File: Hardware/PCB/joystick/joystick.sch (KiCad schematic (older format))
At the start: 38 parts, among them J1 Synth_power_2x5, J2 3_pin_Molex_connector, J3 2_pin_Molex_connector, J4 AudioJack2, J5 6 pin Molex header, J6 AudioJack2, J7 3_pin_Molex_header, J8 2_pin_Molex_header, U1 TL074

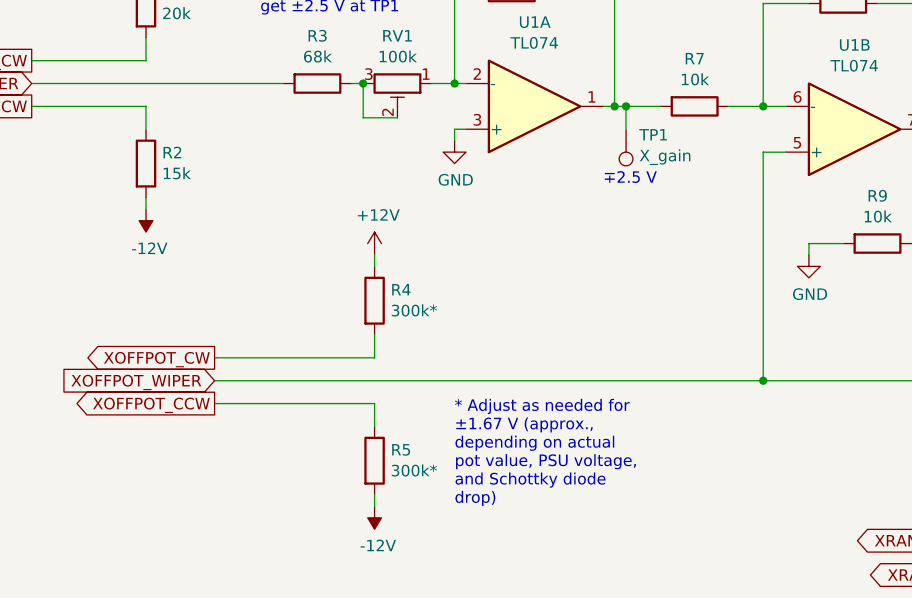
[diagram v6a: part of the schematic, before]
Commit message: Correct resistor value
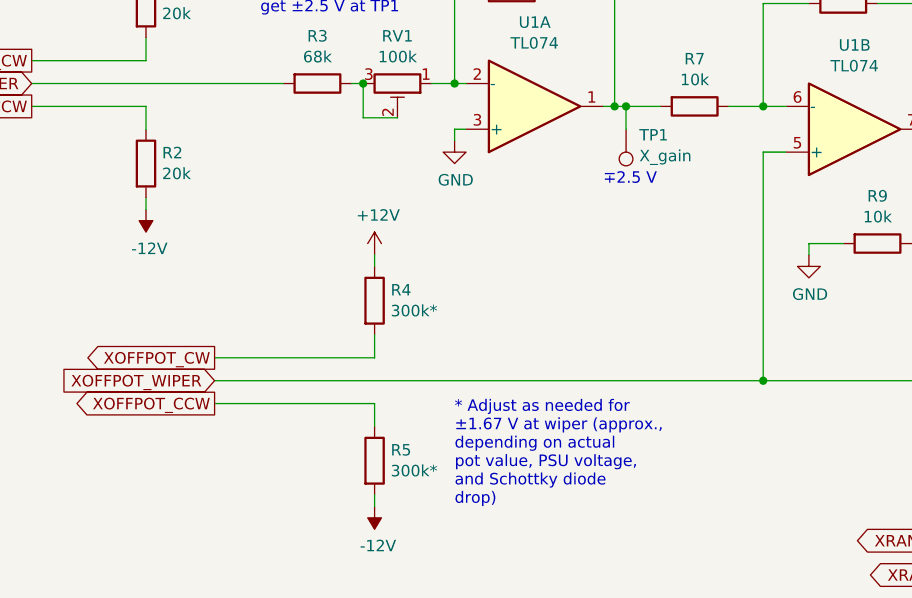
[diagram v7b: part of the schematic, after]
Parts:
- R2: value 15k -> 20k
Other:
- note added: "* Adjust as needed for\n±1.67 V at wiper (approx.,\ndepending on actual\npot value, PSU voltage,\nand Schottky diode\ndrop)"
- note removed: "* Adjust as needed for\n±1.67 V (approx.,\ndepending on actual\npot value, PSU voltage,\nand Schottky diode\ndrop)"
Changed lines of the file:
@@
 P 1600 2350
 F 0 "R2" H 1670 2396 50  0000 L CNN
-F 1 "15k" H 1670 2305 50  0000 L CNN
+F 1 "20k" H 1670 2305 50  0000 L CNN
 F 2 "ao_tht:R_Axial_DIN0207_L6.3mm_D2.5mm_P10.16mm_Horizontal" V 1530 2350 50  0001 C CNN
 F 3 "~" H 1600 2350 50  0001 C CNN
@@
 Check pot for reasonably\naccurate 100k from \npin 1 to 3 or compensate\nby adjusting fixed\nresistors.\n
 Text Notes 2950 3850 0    50   ~ 0
-* Adjust as needed for\n±1.67 V (approx.,\ndepending on actual\npot value, PSU voltage,\nand Schottky diode\ndrop)
+* Adjust as needed for\n±1.67 V at wiper (approx.,\ndepending on actual\npot value, PSU voltage,\nand Schottky diode\ndrop)
 $EndSCHEMATC

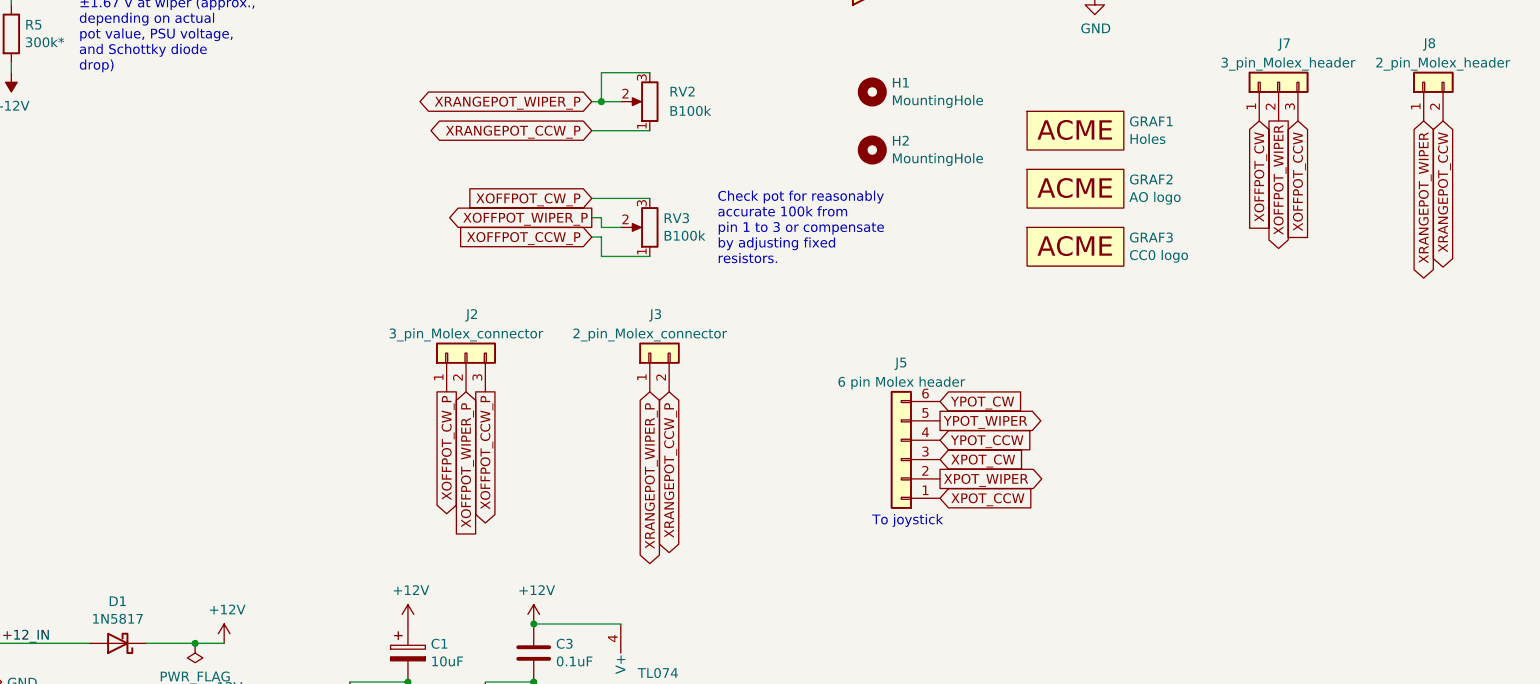
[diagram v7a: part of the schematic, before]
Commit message: Fix wrong R value; update documentation; images
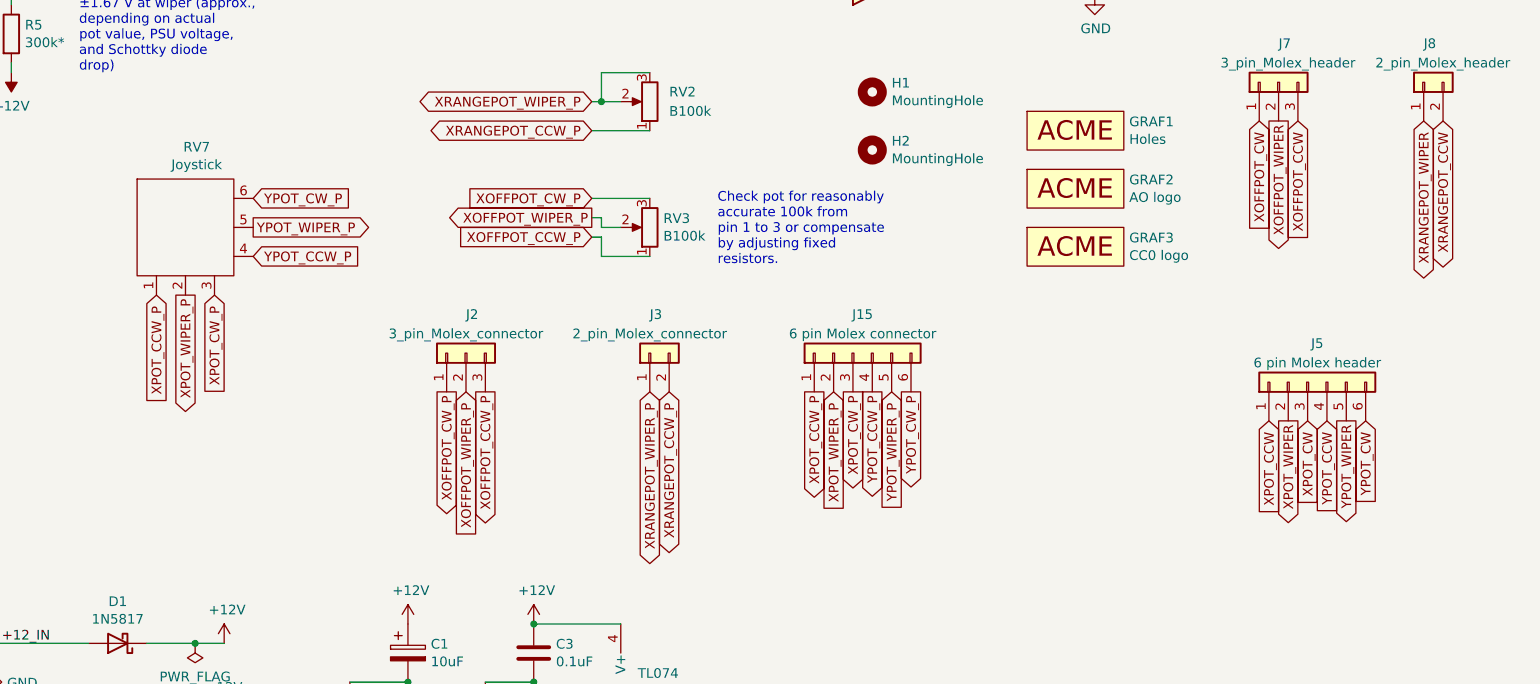
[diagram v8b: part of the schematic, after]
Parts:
- added J15: 6 pin Molex connector, Connector_Molex:Molex_KK-254_AE-6410-06A_1x06_P2.54mm_Vertical, symbol Connector_Generic:Conn_01x06
- added RV7: Joystick, symbol joystick:Joystick
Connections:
- new net XPOT_CCW_P: J15.1 (Pin_1), RV7.1
- new net XPOT_CW_P: J15.3 (Pin_3), RV7.3
- new net XPOT_WIPER_P: J15.2 (Pin_2), RV7.2
- new net YPOT_CCW_P: J15.4 (Pin_4), RV7.4
- new net YPOT_CW_P: J15.6 (Pin_6), RV7.6
- new net YPOT_WIPER_P: J15.5 (Pin_5), RV7.5
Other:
- note removed: "To joystick"
- moved on the sheet: J5
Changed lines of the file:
@@
 L Connector_Generic:Conn_01x06 J5
 U 1 1 5FC3342B
-P 7200 5850
-F 0 "J5" H 7200 5350 50  0000 C CNN
-F 1 "6 pin Molex header" H 7200 5450 50  0000 C CNN
-F 2 "Connector_Molex:Molex_KK-254_AE-6410-06A_1x06_P2.54mm_Vertical" H 7200 5850 50  0001 C CNN
-F 3 "~" H 7200 5850 50  0001 C CNN
-F 4 "Tayda" H 7200 5850 50  0001 C CNN "Vendor"
-	1    7200 5850
-	-1   0    0    1
+P 9300 5450
+F 0 "J5" V 9500 5400 50  0000 C CNN
+F 1 "6 pin Molex header" V 9400 5400 50  0000 C CNN
+F 2 "Connector_Molex:Molex_KK-254_AE-6410-06A_1x06_P2.54mm_Vertical" H 9300 5450 50  0001 C CNN
+F 3 "~" H 9300 5450 50  0001 C CNN
+F 4 "Tayda" H 9300 5450 50  0001 C CNN "Vendor"
+	1    9300 5450
+	0    -1   -1   0
 $EndComp
 Wire Wire Line
@@
 Text GLabel 1100 2100 0    50   Output ~ 0
 XPOT_CCW
-Text GLabel 7400 5850 2    50   Input ~ 0
+Text GLabel 9300 5650 3    50   Input ~ 0
 XPOT_CW
-Text GLabel 7400 5950 2    50   Output ~ 0
+Text GLabel 9200 5650 3    50   Output ~ 0
 XPOT_WIPER
-Text GLabel 7400 6050 2    50   Input ~ 0
+Text GLabel 9100 5650 3    50   Input ~ 0
 XPOT_CCW
-Text GLabel 7400 5550 2    50   Input ~ 0
+Text GLabel 9600 5650 3    50   Input ~ 0
 YPOT_CW
-Text GLabel 7400 5650 2    50   Output ~ 0
+Text GLabel 9500 5650 3    50   Output ~ 0
 YPOT_WIPER
-Text GLabel 7400 5750 2    50   Input ~ 0
+Text GLabel 9400 5650 3    50   Input ~ 0
 YPOT_CCW
-Text Notes 7050 6200 0    50   ~ 0
-To joystick
 Text GLabel 9050 4100 3    50   Input ~ 0
 XOFFPOT_CW
@@
 Text Notes 2950 3850 0    50   ~ 0
 * Adjust as needed for\n±1.67 V at wiper (approx.,\ndepending on actual\npot value, PSU voltage,\nand Schottky diode\ndrop)
+$Comp
+L Connector_Generic:Conn_01x06 J15
+U 1 1 61A72ED0
+P 6950 5300
+F 0 "J15" V 7150 5250 50  0000 C CNN
+F 1 "6 pin Molex connector" V 7050 5250 50  0000 C CNN
+F 2 "Connector_Molex:Molex_KK-254_AE-6410-06A_1x06_P2.54mm_Vertical" H 6950 5300 50  0001 C CNN
+F 3 "~" H 6950 5300 50  0001 C CNN
+F 4 "Tayda" H 6950 5300 50  0001 C CNN "Vendor"
+	1    6950 5300
+	0    -1   -1   0
+$EndComp
+Text GLabel 6950 5500 3    50   Output ~ 0
+XPOT_CW_P
+Text GLabel 6850 5500 3    50   Input ~ 0
+XPOT_WIPER_P
+Text GLabel 6750 5500 3    50   Output ~ 0
+XPOT_CCW_P
+Text GLabel 7250 5500 3    50   Output ~ 0
+YPOT_CW_P
+Text GLabel 7150 5500 3    50   Input ~ 0
+YPOT_WIPER_P
+Text GLabel 7050 5500 3    50   Output ~ 0
+YPOT_CCW_P
+$Comp
+L joystick:Joystick RV7
+U 1 1 61A7D383
+P 3500 4650
+F 0 "RV7" H 3558 5065 50  0000 C CNN
+F 1 "Joystick" H 3558 4974 50  0000 C CNN
+F 2 "" H 3500 4650 50  0001 C CNN
+F 3 "" H 3500 4650 50  0001 C CNN
+	1    3500 4650
+	1    0    0    -1
+$EndComp
+Text GLabel 3650 5000 3    50   Input ~ 0
+XPOT_CW_P
+Text GLabel 3500 5000 3    50   Output ~ 0
+XPOT_WIPER_P
+Text GLabel 3350 5000 3    50   Input ~ 0
+XPOT_CCW_P
+Text GLabel 3850 4500 2    50   Input ~ 0
+YPOT_CW_P
+Text GLabel 3850 4650 2    50   Output ~ 0
+YPOT_WIPER_P
+Text GLabel 3850 4800 2    50   Input ~ 0
+YPOT_CCW_P
 $EndSCHEMATC
